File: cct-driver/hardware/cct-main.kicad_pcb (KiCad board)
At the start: 2 copper layers, 110 x 145 mm, 205 parts, among them J1 C707824, J10 C37815, J11 C474923, J2 C165948, J3 C441333, J4 C441333, J5 C441333, J6 C441333, J7 C441333, J8 C441333, J9 C2906270, Q1 C3281500, Q10 C2890395, Q11 C2890395, Q12 C2890395, Q13 C2890395, Q14 C2890395, Q15 C2890395, Q16 C2890395, Q17 C2890395, Q18 C2890395, Q2 C3281500, Q3 C20526, Q4 C2146, Q5 C2146, Q6 C20526, Q7 C2890395, Q8 C2890395, Q9 C2890395, SW1 C318884, SW2 C318884, U1 C2864837, U2 C524806, U3 C6186, U4 C701341, U5 C84681, U6 C52140501, U7 C52140501

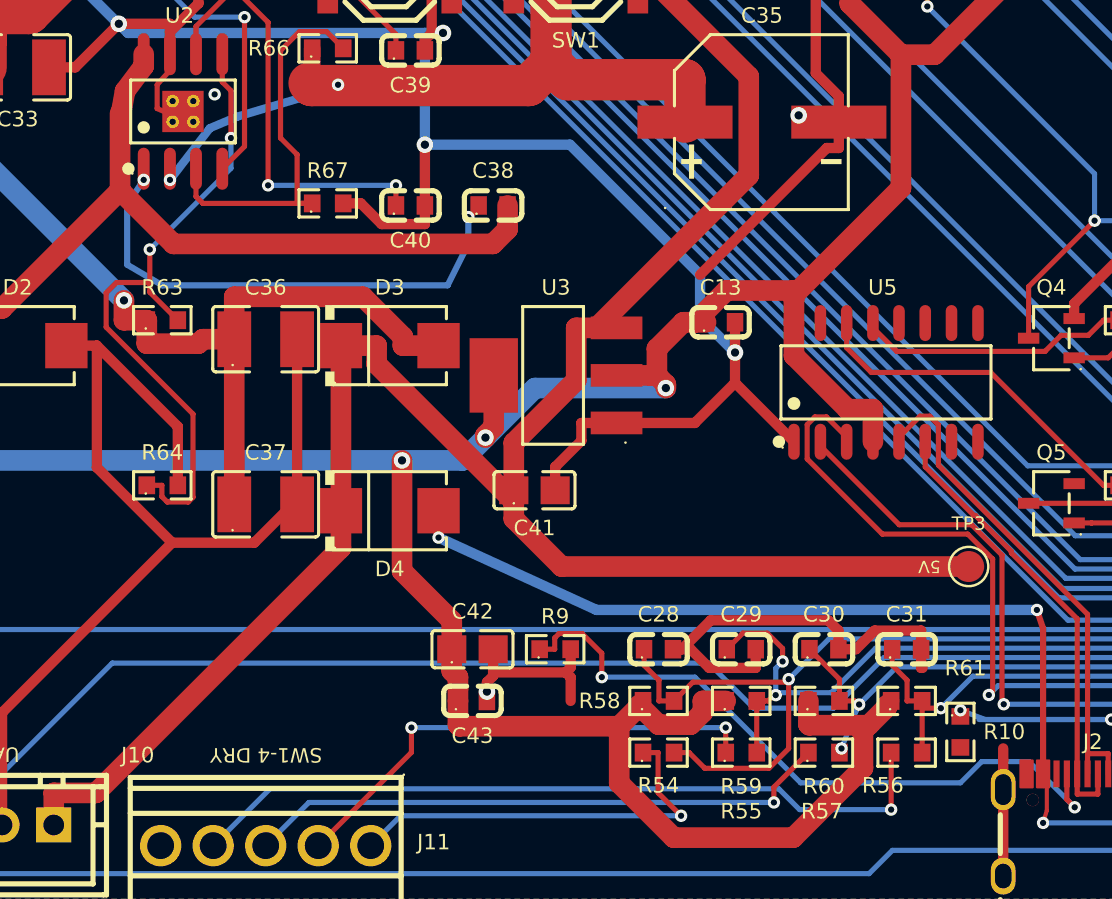
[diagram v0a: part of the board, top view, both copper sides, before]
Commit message: fix(hw): 5 个压在贴片焊盘下的过孔挪出焊盘,本批就改
嘉立创 SMT DFM「元件焊脚到孔」里孔腔/锡量最差的 5 个:U2.1(BOOT)、
U2.2(V24_LOGIC)、R56.2(SW_IN3)、R10.1(CC2)、C43.2(GND)。原判定是
「本批放行、下一版再改」,兜底是「烙铁一点就补上」—— 本项目立项前提是
用户零焊接(为此砍掉调试排针、全部选预焊件),这个兜底不成立,所以本批改。

后果不对称:BOOT 虚焊 = buck 不起振 = 5V/3.3V 全没;R10 是 USB-C 的 CC2
下拉,开路就只有一个插入方向能枚举,而刷固件全靠这个口。

判定口径:孔口离开该焊盘铜面 ≥0.30mm。只动这 5 个孔的位置和各自的引出线,
元件位置、焊盘尺寸、网络拓扑一个没动,其余 28 处压孔一处未碰。

U2.1(BOOT) 往上挪而不是往下:下方那块空当被 SW_NODE 的 1mm 走线和 FB_5V
斜线夹成三角缝,BOOT 与 V24_LOGIC 两颗孔挤不进去(网格搜索最好组合裕量 0.00mm)。
代价是 BOOT 走线 23.4→26.0mm;这条回路本来就有 16mm(自举电容 C38 的既有位置),
+2.6mm 远小于 BOOT 脚虚焊的风险。

压孔 33→28(少的正好是这 5 个,0 处新增,两套判据互相印证);
DRC 89→89 逐条一致、新增 0 消失 0;未连接项 0。覆铜已重灌
(不重灌新孔位会落在原 GND 铜面里)。全程命令行,没开图形界面。

Co-Authored-By: Claude <noreply@anthropic.com>
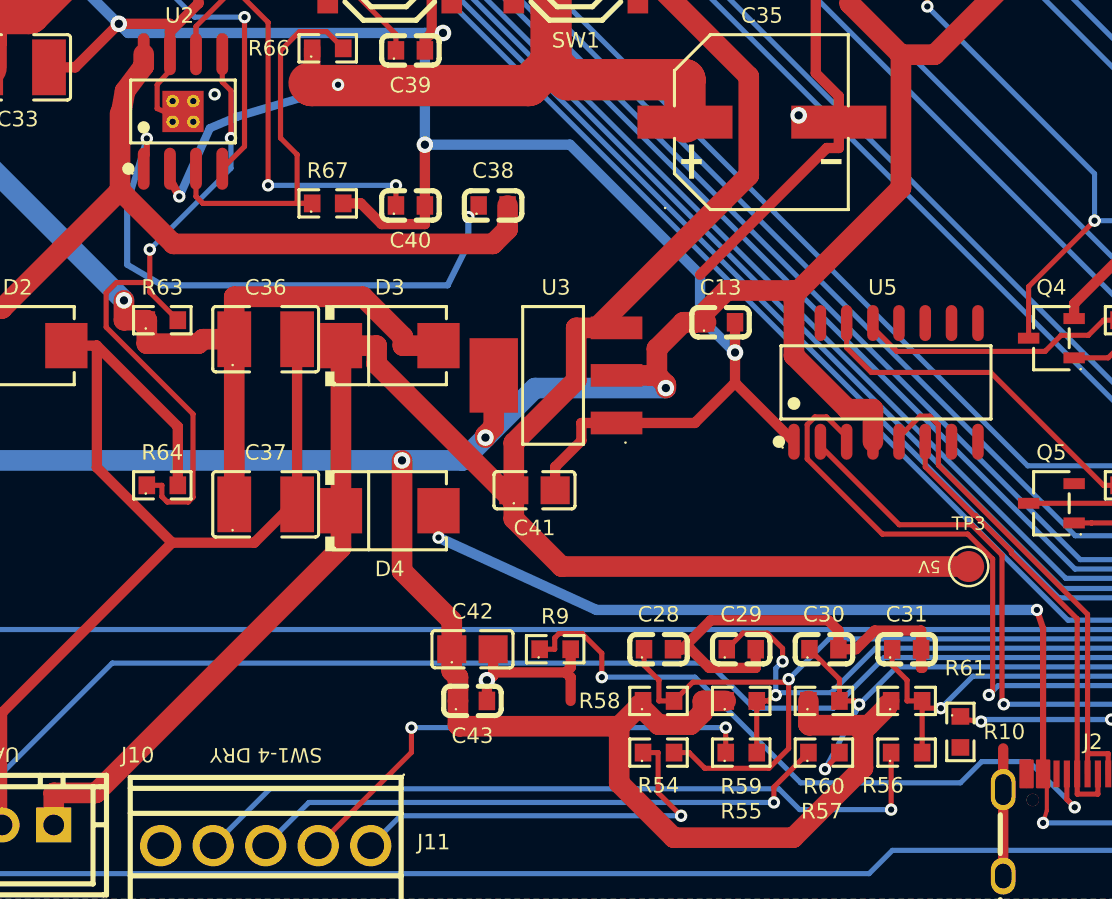
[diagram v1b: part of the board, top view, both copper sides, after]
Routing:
- net BOOT: track 24.5 -> 27.1 mm
- net SW_IN3: track 50.1 -> 52.0 mm
- net V24_LOGIC: track 92.7 -> 93.8 mm
- net CC2: track 16.8 -> 16.2 mm
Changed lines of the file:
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@@
 	)
 	(segment
+		(start 31.5 110)
+		(end 31.82 110.6)
+		(width 0.4)
+		(layer "F.Cu")
+		(net "V24_LOGIC")
+	)
+	(segment
 		(start 50.602 104.9553)
 		(end 49.8029 104.1562)
@@
 	)
 	(via
-		(at 31.37 109.8)
+		(at 31.82 110.6)
 		(size 0.6)
 		(drill 0.3)
@@
 	)
 	(segment
-		(start 31.37 109.8)
+		(start 31.82 110.6)
 		(end 33.299999 107.3)
 		(width 0.4)
@@
 	(segment
 		(start 47 133.7983)
-		(end 46.7 134.0983)
+		(end 46.7 134)
 		(width 0.5)
 		(layer "F.Cu")
@@
 	(segment
 		(start 46.7 135)
-		(end 46.7 134.0983)
+		(end 46.7 134)
 		(width 0.5)
 		(layer "F.Cu")
@@
 	)
 	(via
-		(at 46.7 134.55)
+		(at 46.7 134)
 		(size 0.8)
 		(drill 0.4)
@@
 	)
 	(segment
-		(start 62.3 132.5)
-		(end 63.75 133.95)
+		(start 63.6 137.7)
+		(end 63.05 138.3)
 		(width 0.25)
 		(layer "F.Cu")
@@
 	)
 	(segment
-		(start 63.8 137.5)
-		(end 63.85 137.32)
+		(start 62.3 132.5)
+		(end 63.75 133.95)
 		(width 0.25)
 		(layer "F.Cu")
@@
 	)
 	(via
-		(at 63.85 137.3)
+		(at 63.05 138.3)
 		(size 0.6)
 		(drill 0.3)
@@
 	)
 	(segment
-		(start 63.85 137.3)
+		(start 63.05 138.3)
 		(end 64.55 135.5)
 		(width 0.25)
@@
 		(net "BOOT")
 	)
+	(segment
+		(start 30.25 108.6)
+		(end 30.25 107.8)
+		(width 0.3)
+		(layer "F.Cu")
+		(net "BOOT")
+	)
 	(via
 		(at 45.8 111.6)
@@
 	)
 	(via
-		(at 30.1 109.8)
+		(at 30.25 107.8)
 		(size 0.6)
 		(drill 0.3)
@@
 	)
 	(segment
-		(start 30.1 109.8)
+		(start 30.25 107.8)
 		(end 29.3 111)
 		(width 0.3)
@@
 	)
 	(segment
-		(start 69.6 135.75)
-		(end 69.6 135.45)
+		(start 69.85 135.9)
+		(end 70.6 136)
 		(width 0.25)
 		(layer "F.Cu")
@@
 	)
 	(via
-		(at 69.6 135.45)
+		(at 70.6 136)
 		(size 0.6)
 		(drill 0.3)
@@
 	)
 	(segment
-		(start 69.6 135.45)
+		(start 70.6 136)
 		(end 70.8 135.9)
 		(width 0.25)

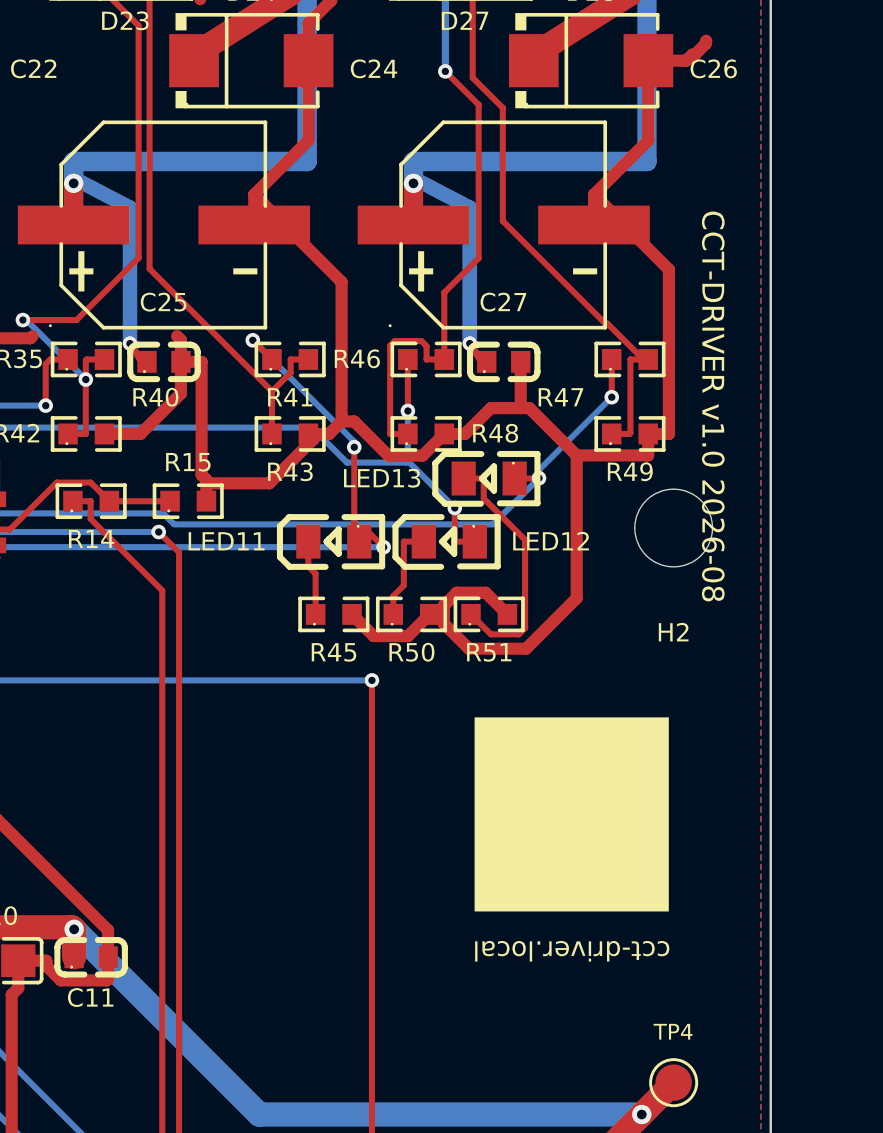
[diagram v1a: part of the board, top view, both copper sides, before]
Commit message: 丝印：板名改成 PendingHome CCT LED Driver 1，挪到白油块下方横排
三处改动，只碰 F.Silkscreen：

1. 板名 `CCT-DRIVER v1.0 2026-08` → `PendingHome CCT LED Driver 1`。
2. 删掉白油块正下方那行明码 `cct-driver.local`（人类不要了）。
3. 板名从右缘 270° 竖排改成 180° 横排，放到刚空出来的白油块下方，
   中心 (96.8, 98.0)，包围盒 85.86–107.74 / 97.16–98.84。
   这样全板 237 条丝印文字里只剩保险丝那一条还是 270°。

保险丝那条 `FUSE 4A-T x6 / MAIN 15A` 保持 270° 不动：横排要 16.61mm
（含 0.3mm 净空共 17.21mm），而保险丝区 y13–36 整个带子里最长的空档只有
10.38mm（还在 F1 保险丝座内框里），塞不下，硬塞会压别的丝印。

新板名字高 0.9mm、线宽 0.18mm，都过嘉立创下限（0.8 / 0.15）；最近障碍是
TP4 的位号，距 1.34mm，离板边最近 2.26mm。白油块（8×8mm，97.8–105.8 /
87.8–95.8）原样未动。

DRC 89 → 88 条，逐条比对新增 0；少的那条是旧竖排板名被 H2 安装孔阻焊
开窗切到（silk_over_copper），挪走后自然消失。

Co-Authored-By: Claude <noreply@anthropic.com>
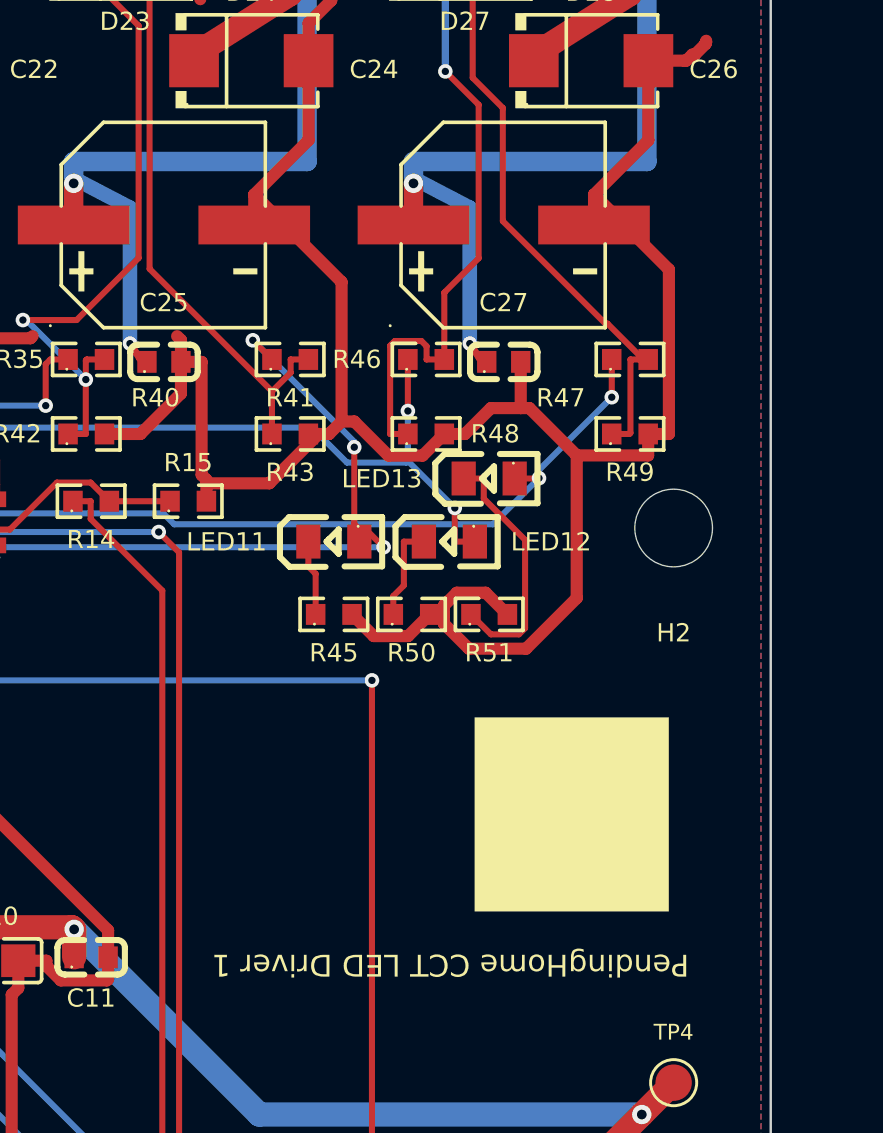
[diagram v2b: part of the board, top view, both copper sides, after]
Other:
- board text added: "PendingHome CCT LED Driver 1"
- board text removed: "CCT-DRIVER v1.0 2026-08"
- board text removed: "cct-driver.local"
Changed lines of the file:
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@@
-		)
-	)
-	(gr_text "cct-driver.local"
-		(at 101.8 97.4 180)
-		(layer "F.SilkS")
-		(effects
-			(font
-				(size 0.8 0.8)
-				(thickness 0.13)
-			)
 		)
 	)
@@
 		)
 	)
-	(gr_text "CCT-DRIVER v1.0 2026-08"
-		(at 107.6 75 270)
+	(gr_text "PendingHome CCT LED Driver 1"
+		(at 96.8 98 180)
 		(layer "F.SilkS")
 		(effects

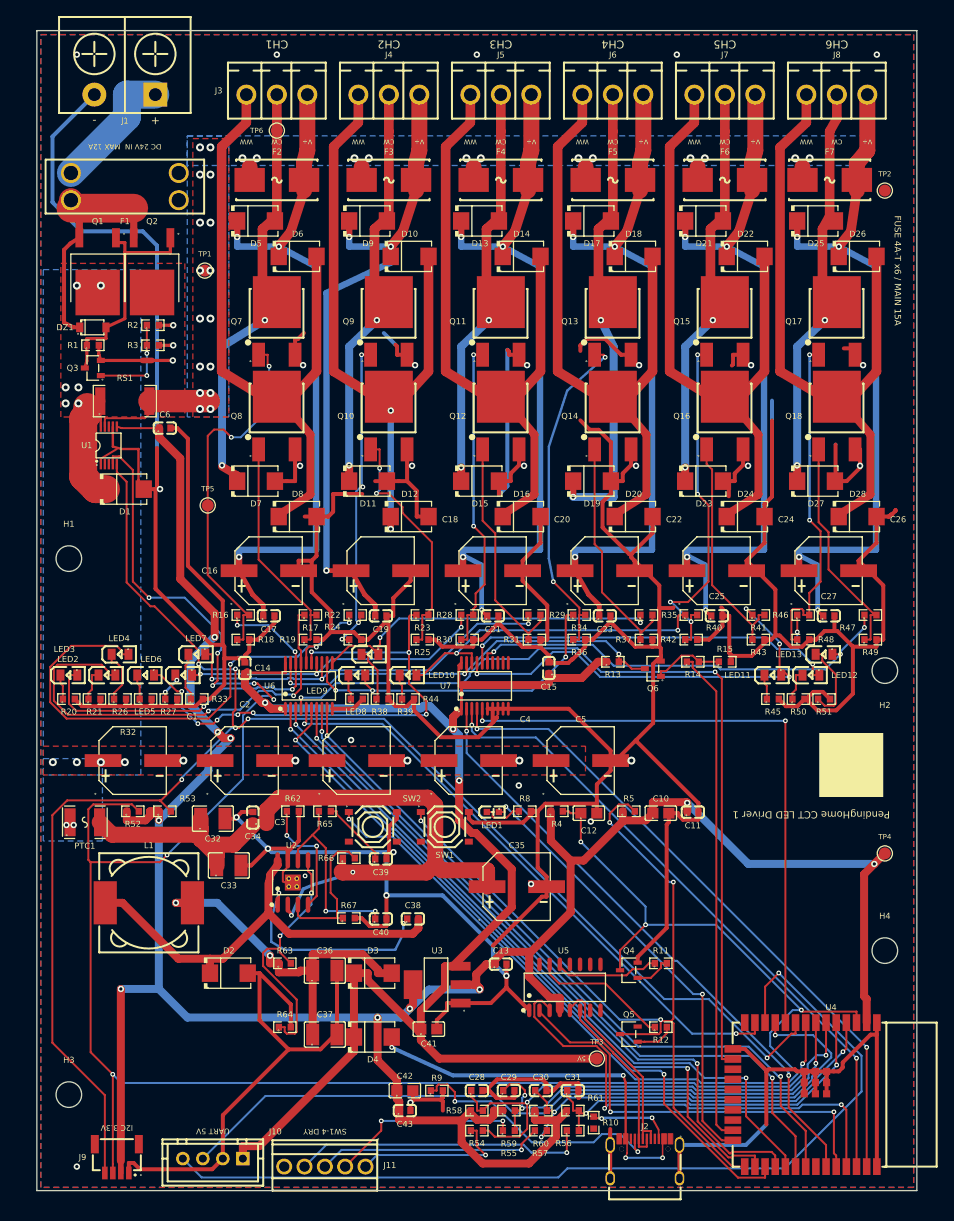
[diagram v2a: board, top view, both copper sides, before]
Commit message: 整板转正:文件坐标系改成上墙姿态,位号不再倒着印
丝印方向的坑一直是"文件正着画、板子倒着装",靠把文字预转 180° 来补偿。
但 KiCad 对封装自带文字有 keep-upright 保护,绘图时会把倒过来的位号又扶正
——于是 33 条独立标注转过去了、205 个位号没转,出货 Gerber 里位号在安装
姿态下是倒的。之前那版只是把文字转了个方向,没治本。

治本做法是把整块板绕板心 (55, 72.5) 转 180°:封装 205 / 走线过孔 2191 /
图形文字 38 / 覆铜 9 全部跟着转。此后**文件里看到的方向就是装上墙看到的
方向**(接线端子在下方),所有丝印文字回归自然角度——位号 0°、横排标注 0°、
右缘那条 FUSE 竖排标注转到左缘 90°。不需要任何人工补偿,keep-upright
也原样保留着没动。

板框正好 0–110 × 0–145,绕板心 180° 自映射,原点与尺寸都不变。

物理上真正改变的只有 205 个位号相对铜箔转了 180°,这正是要修的那件事。
verify_rotate180.py 是配套的安全网:把新导出的每一层坐标旋转回去与旧包
比对——B_Cu / B_Mask / B_Paste / B_Silkscreen 逐字节相同;F_Cu / F_Mask /
F_Paste / Edge_Cuts 点集完全一致(差异只有 J2 那三个自由多边形光圈的
实例化角度 0°→180°,以及板框四条边的书写顺序);PTH 327 个孔在 nm 精度
上完全一致,钻孔文件里 21 个孔差 1µm 纯粹是 0.001mm 打印精度的舍入。
DRC 88 条违规,分类逐项与旧板一致(丝印三类 53/10/9 一条没多)。

Co-Authored-By: Claude <noreply@anthropic.com>
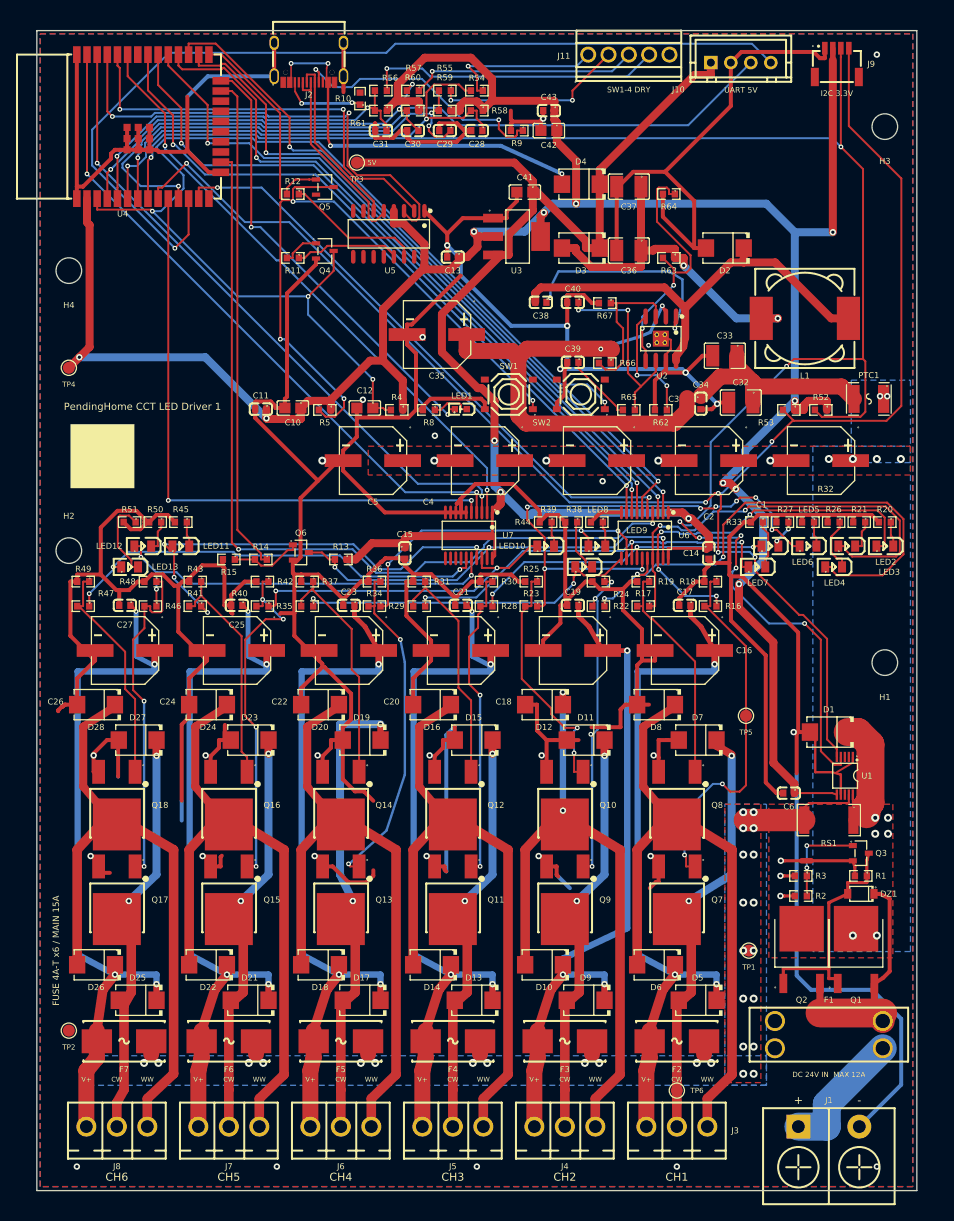
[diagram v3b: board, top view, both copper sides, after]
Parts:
- moved J9 163.9 mm to (100.0, 4.00), turned to 0 degrees
- moved H3 158.3 mm to (106.0, 12.0), turned to 180 degrees
- moved J8 157.3 mm to (10.0, 137.0), turned to 0 degrees
- moved J1 156.2 mm to (99.0, 137.0), turned to 0 degrees
- moved J10 152.1 mm to (88.0, 4.00), turned to 0 degrees
- moved TP2 146.4 mm to (4.00, 125.0), turned to 180 degrees
- moved U4 146.2 mm to (14.0, 12.0), turned to 0 degrees
- moved J11 144.1 mm to (74.0, 3.00), turned to 0 degrees
- moved J2 143.3 mm to (34.0, 4.00), turned to 180 degrees
- moved J7 143.1 mm to (24.0, 137.0), turned to 0 degrees
- moved F7 139.2 mm to (10.9, 126.3), turned to 180 degrees
- moved J3 138.4 mm to (80.0, 137.0), turned to 0 degrees
- moved F1 137.8 mm to (99.0, 125.5), turned to 180 degrees
- moved J6 133.4 mm to (38.0, 137.0), turned to 0 degrees
- moved H4 132.8 mm to (4.00, 30.0), turned to 180 degrees
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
